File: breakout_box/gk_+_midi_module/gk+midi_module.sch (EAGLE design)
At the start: 114 parts, among them T1 2N2222, T2 2N2222, U2 LMV324, U3 TLV2170DGKT, U4 L78LXX, U5 MIC5205-3.3, U6B MSP430G2553RHB32, X1 QUARZ5

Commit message: update schematics
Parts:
- renumbered U6B to U6
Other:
- note added: "(AUX3)"
- note added: "(AUX4)"
- note added: "(AUX5)"
- note added: "(AUX6)"
- note added: "13 PIN CONNECTOR"
- note added: "MCU MODULE"
- note added: "P2.1 (AUX1)"
- note added: "P2.2 (AUX2)"
- note removed: "MSP430G2553RHB32"
- note removed: "U6A"

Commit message: update gk+midi files
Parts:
- removed JP1: (no value), pinhead-2:PINHD-1X03_2.00
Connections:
- net CH7_SW renamed CH7_MIDI_SW
- net CH8_SW renamed CH8_MIDI_SW
- removed net N$10: C3.1, JP1.3, R1.2, U1G$1.IN+
- removed net N$4: H3.3, JP1.2
- net CH10_GK_VOL: now also C3.1, H3.3, R1.2, U1G$1.IN+; no longer JP1.1
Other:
- note added: "CH7_SW"
- note added: "CH8_SW"
- note added: "CH9_SW"
- note removed: "CH7_GK_SW/CV"
- note removed: "CH8_GK_SW/CV"
- note removed: "CH9_CV"

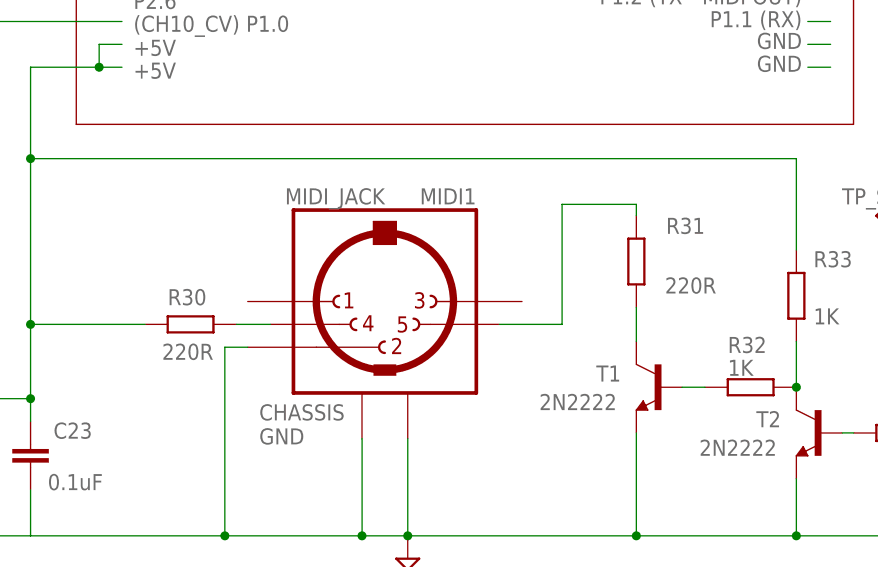
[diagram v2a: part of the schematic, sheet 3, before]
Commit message: Update brd and sch file with corrected footprints
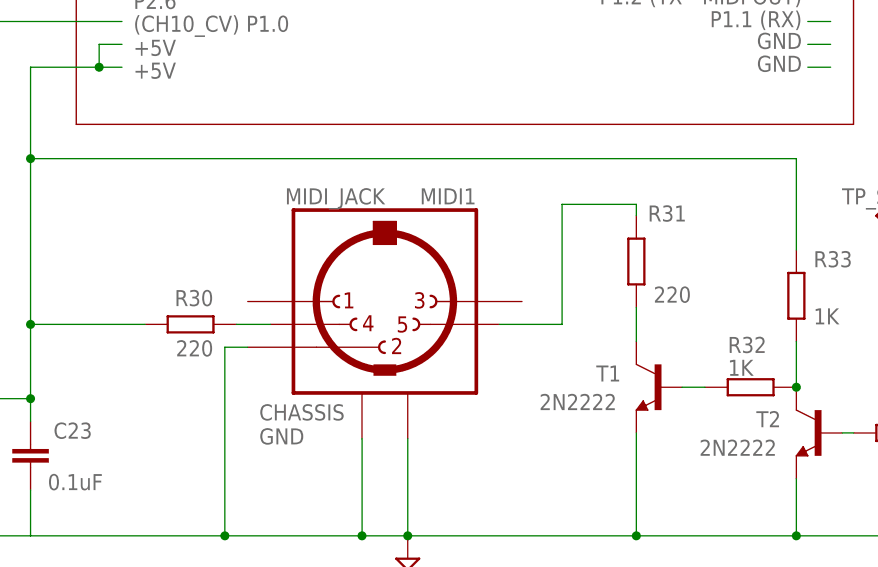
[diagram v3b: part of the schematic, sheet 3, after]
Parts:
- C17, C18: device resistor:C-EUC0402 -> resistor:C-EUC0603
- R30, R31: value 220R -> 220; device resistor:R-EU_R0603 -> resistor:R-EU_R0402
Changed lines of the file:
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@@
 <part name="H6" library="con-lstb" deviceset="MA08-1" device="" value="DNP"/>
 <part name="H7" library="con-lstb" deviceset="MA08-1" device="" value="DNP"/>
-<part name="R30" library="resistor" deviceset="R-EU_" device="R0603" value="220R"/>
-<part name="R31" library="resistor" deviceset="R-EU_" device="R0603" value="220R"/>
 <part name="C35" library="resistor" deviceset="C-EU" device="C0402" value="1nF"/>
 <part name="C30" library="resistor" deviceset="C-EU" device="C0402" value="1uF"/>
@@
 <part name="C15" library="resistor" deviceset="C-EU" device="C0603" value="4.7uF"/>
 <part name="C16" library="resistor" deviceset="C-EU" device="C0603" value="4.7uF"/>
-<part name="C17" library="resistor" deviceset="C-EU" device="C0402" value="0.1uF"/>
-<part name="C18" library="resistor" deviceset="C-EU" device="C0402" value="0.1uF"/>
 <part name="C14" library="resistor" deviceset="C-EU" device="C0402" value="0.01uF"/>
 <part name="R13" library="resistor" deviceset="R-EU_" device="R0402" value="5.1k"/>
@@
 <part name="FRAME6" library="frames" deviceset="DINA4_L" device=""/>
 <part name="U$1" library="CYCFI_Con" deviceset="13P_MIDI_2" device=""/>
+<part name="R30" library="resistor" deviceset="R-EU_" device="R0402" value="220"/>
+<part name="R31" library="resistor" deviceset="R-EU_" device="R0402" value="220"/>
+<part name="C17" library="resistor" deviceset="C-EU" device="C0603" value="0.1uF"/>
+<part name="C18" library="resistor" deviceset="C-EU" device="C0603" value="0.1uF"/>
 </parts>
 <sheets>
@@
 <attribute name="VALUE" x="237.109" y="137.541" size="1.778" layer="96"/>
 </instance>
-<instance part="C17" gate="G$1" x="252.095" y="161.29" smashed="yes">
-<attribute name="NAME" x="253.619" y="161.671" size="1.778" layer="95"/>
-<attribute name="VALUE" x="253.619" y="156.591" size="1.778" layer="96"/>
-</instance>
-<instance part="C18" gate="G$1" x="252.095" y="142.24" smashed="yes">
-<attribute name="NAME" x="253.619" y="142.621" size="1.778" layer="95"/>
-<attribute name="VALUE" x="253.619" y="137.541" size="1.778" layer="96"/>
-</instance>
 <instance part="C14" gate="G$1" x="102.87" y="124.46" smashed="yes">
 <attribute name="NAME" x="96.774" y="126.111" size="1.778" layer="95"/>
@@
 </instance>
 <instance part="U$1" gate="G$1" x="184.785" y="88.9"/>
+<instance part="C17" gate="G$1" x="252.095" y="161.29" smashed="yes">
+<attribute name="NAME" x="253.619" y="161.671" size="1.778" layer="95"/>
+<attribute name="VALUE" x="253.619" y="156.591" size="1.778" layer="96"/>
+</instance>
+<instance part="C18" gate="G$1" x="252.095" y="142.24" smashed="yes">
+<attribute name="NAME" x="253.619" y="142.621" size="1.778" layer="95"/>
+<attribute name="VALUE" x="253.619" y="137.541" size="1.778" layer="96"/>
+</instance>
 </instances>
 <busses>
@@
 <attribute name="TP_SIGNAL_NAME" x="161.29" y="74.93" size="1.778" layer="97" rot="R90"/>
 </instance>
-<instance part="R30" gate="G$1" x="83.82" y="61.595" smashed="yes">
-<attribute name="NAME" x="81.28" y="63.7286" size="1.778" layer="95"/>
-<attribute name="VALUE" x="80.645" y="57.658" size="1.778" layer="96"/>
-</instance>
-<instance part="R31" gate="G$1" x="133.35" y="68.58" smashed="yes" rot="R90">
-<attribute name="NAME" x="140.97" y="73.4314" size="1.778" layer="95" rot="R180"/>
-<attribute name="VALUE" x="142.24" y="66.802" size="1.778" layer="96" rot="R180"/>
-</instance>
 <instance part="R24" gate="G$1" x="40.64" y="154.94" smashed="yes">
 <attribute name="NAME" x="39.37" y="158.75" size="1.778" layer="95" rot="R180"/>
@@
 <attribute name="VALUE" x="196.85" y="62.23" size="1.778" layer="96" rot="R180"/>
 </instance>
+<instance part="R30" gate="G$1" x="83.82" y="61.595" smashed="yes">
+<attribute name="NAME" x="86.36" y="65.405" size="1.778" layer="95" rot="R180"/>
+<attribute name="VALUE" x="86.36" y="59.817" size="1.778" layer="96" rot="R180"/>
+</instance>
+<instance part="R31" gate="G$1" x="133.35" y="68.58" smashed="yes" rot="R90">
+<attribute name="NAME" x="134.62" y="73.025" size="1.778" layer="95"/>
+<attribute name="VALUE" x="135.255" y="64.008" size="1.778" layer="96"/>
+</instance>
 </instances>
 <busses>
@@
 <pinref part="C23" gate="G$1" pin="1"/>
 <wire x1="66.04" y1="53.34" x2="66.04" y2="50.8" width="0.1524" layer="91"/>
-<pinref part="R30" gate="G$1" pin="1"/>
 <wire x1="66.04" y1="53.34" x2="66.04" y2="61.595" width="0.1524" layer="91"/>
 <wire x1="66.04" y1="61.595" x2="78.74" y2="61.595" width="0.1524" layer="91"/>
@@
 <label x="77.47" y="91.44" size="1.778" layer="95"/>
 <label x="77.47" y="88.9" size="1.778" layer="95"/>
+<pinref part="R30" gate="G$1" pin="1"/>
 </segment>
 <segment>

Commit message: changed some resistors to 0603
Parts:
- R22, R23, R30, R31: device resistor:R-EU_R0402 -> resistor:R-EU_R0603
